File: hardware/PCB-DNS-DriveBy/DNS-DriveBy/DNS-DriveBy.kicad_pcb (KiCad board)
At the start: 2 copper layers, 76 x 40 mm, 21 parts, among them J1 JST 2.0, J2 Conn_01x04, J3 Conn_01x03, Q1 2N3904, Q2 2N3904, SW1 SW_SPST, U1 D1 Mini, U2 NEO-6M

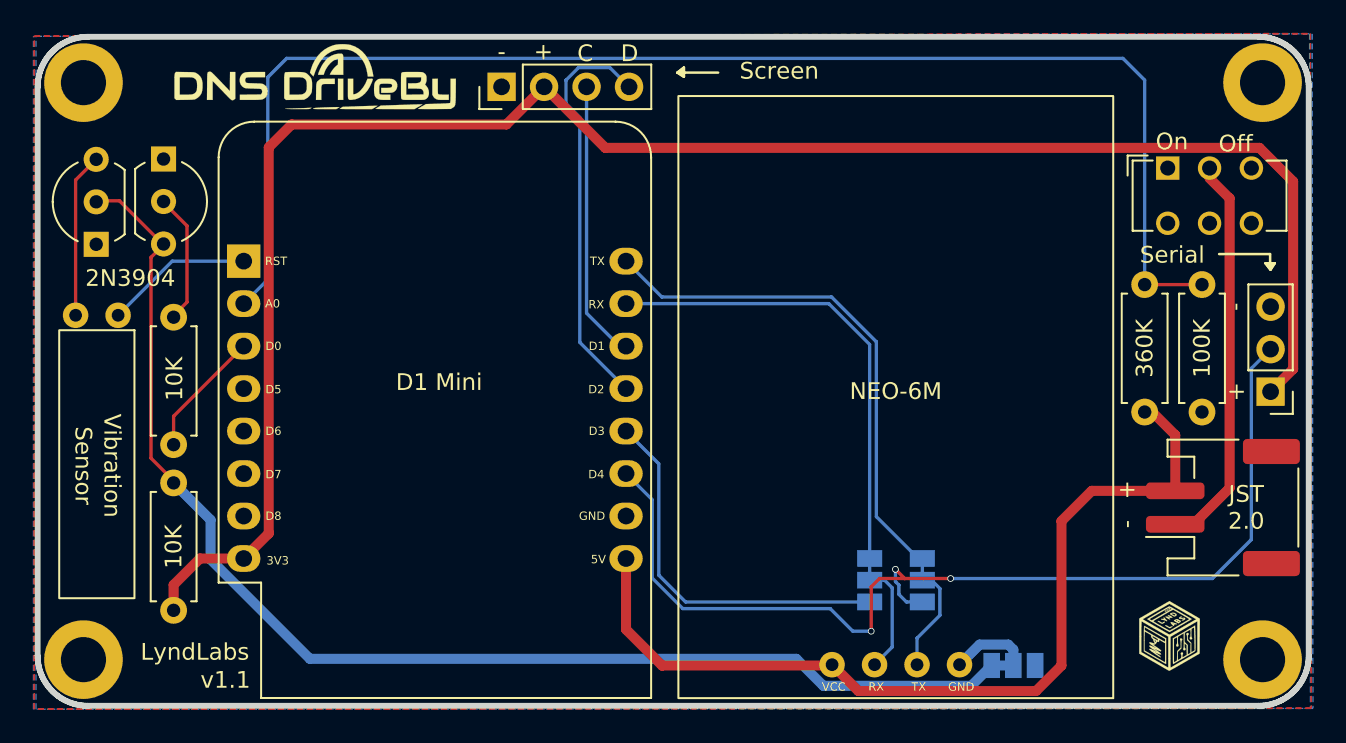
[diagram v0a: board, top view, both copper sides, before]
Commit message: fix low-power mode hardware, add jumper pads, graphics
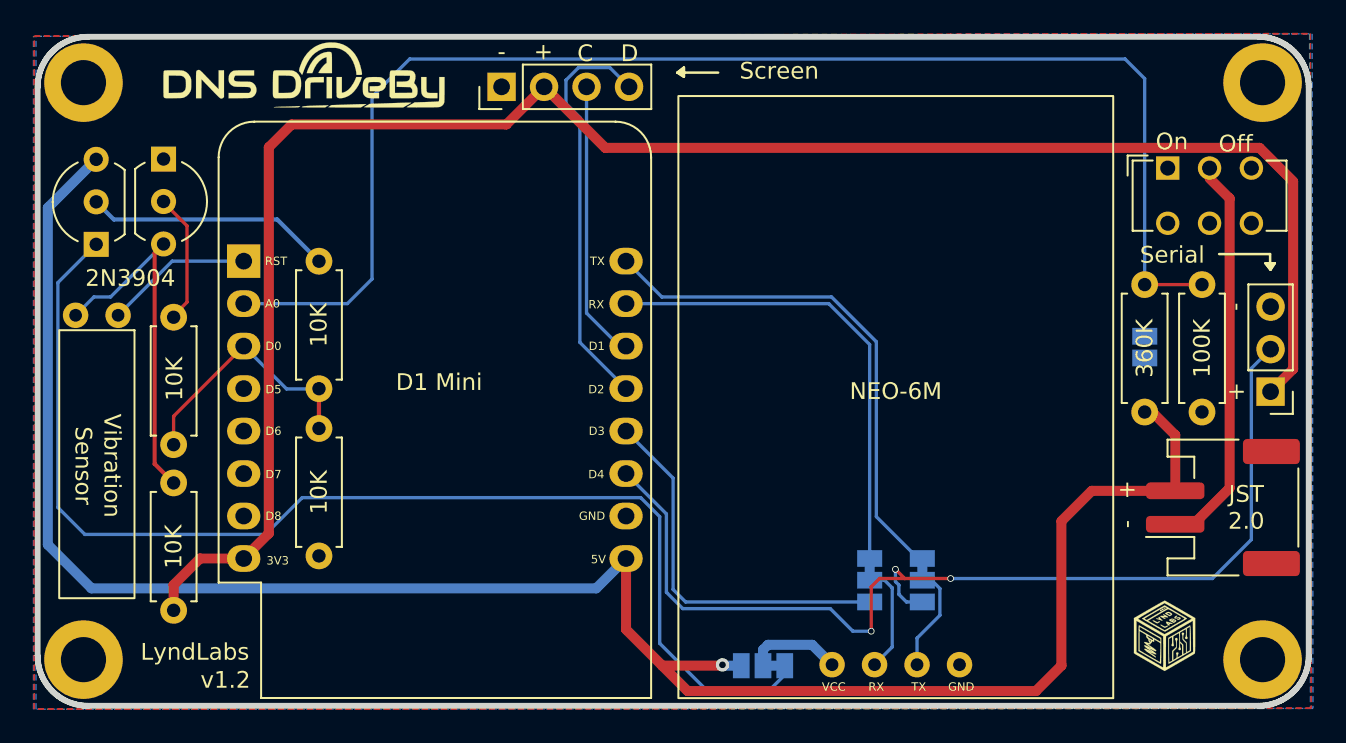
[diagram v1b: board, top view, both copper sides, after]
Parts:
- removed the Ref** at (26.4, 20.1)
- added JP4: Jumper_2_Open, Jumper:SolderJumper-2_P1.3mm_Open_Pad1.0x1.5mm, B.Cu at (67.0, 19.3)
- added R3: 10K, Resistor_THT:R_Axial_DIN0207_L6.3mm_D2.5mm_P7.62mm_Horizontal, F.Cu at (17.6, 31.8)
- added R4: 10K, Resistor_THT:R_Axial_DIN0207_L6.3mm_D2.5mm_P7.62mm_Horizontal, F.Cu at (17.6, 14.2)
- added Ref**: Val**, v1.0-pcb-art, F.Cu at (38.0, 20.5)
- JP1: renamed from GPS GND; value SolderJumper-3_P1.3mm_Open_Pad1.0x1.5mm -> GPS GND; footprint Jumper:SolderJumper-3_P1.3mm_Open_Pad1.0x1.5mm -> Jumper:SolderJumper-3_P1.3mm_Bridged12_Pad1.0x1.5mm
- JP2: renamed from RX; value SolderJumper-3_P1.3mm_Open_Pad1.0x1.5mm -> RX; footprint Jumper:SolderJumper-3_P1.3mm_Open_Pad1.0x1.5mm -> Jumper:SolderJumper-3_P1.3mm_Bridged12_Pad1.0x1.5mm
- JP3: renamed from TX; value SolderJumper-3_P1.3mm_Open_Pad1.0x1.5mm -> TX; footprint Jumper:SolderJumper-3_P1.3mm_Open_Pad1.0x1.5mm -> Jumper:SolderJumper-3_P1.3mm_Bridged12_Pad1.0x1.5mm
- moved JP1 15.0 mm to (44.1, 38.4)
- renumbered R3 to R5, R4 to R6
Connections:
- net TX1 renamed D4
- JP1 pad 1: GND -> Net-(JP1-Pad1)
- JP1 pad 2: GPS- -> Net-(JP1-Pad2)
- JP1 pad 3: GPS- -> +BATT
- JP2 pad 3: unconnected-(U1-Pad12) -> D3
- JP3 pad 2: GPS_TX -> Net-(JP3-Pad2)
- Q1 pad 3: GPS- -> Net-(Q1-Pad3)
- Q2 pad 1: GND -> Net-(JP1-Pad1)
- Q2 pad 2: GPS- -> Net-(Q2-Pad2)
- Q2 pad 3: Net-(Q2-Pad3) -> +BATT
- R2 pad 1: GPS- -> Net-(Q1-Pad3)
- U1 pad 12: unconnected-(U1-Pad12) -> D3
- U2 pad 1: +BATT -> Net-(JP1-Pad2)
- U2 pad 2: GPS_RX -> Net-(JP2-Pad2)
- U2 pad 3: GPS_TX -> Net-(JP3-Pad2)
- U2 pad 4: GPS- -> GND
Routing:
- net GPS-: track 82.0 -> 0.00 mm
- net Net-(JP1-Pad1): track 0.00 -> 71.8 mm
- net +BATT: track 54.6 -> 120.0 mm, vias 0 -> 1
- net unconnected-(U1-Pad12): track 22.7 -> 0.00 mm
- net D3: track 0.00 -> 22.7 mm
- net Net-(Q1-Pad3): track 0.00 -> 22.0 mm
- net Net-(Q2-Pad2): track 0.00 -> 14.8 mm
- net Net-(Q2-Pad3): track 9.83 -> 0.00 mm
- net D0: track 7.53 -> 15.5 mm
- net GPS_TX: track 38.9 -> 31.2 mm
- net GPS_RX: track 35.9 -> 28.4 mm
- net Net-(JP3-Pad2): track 0.00 -> 6.37 mm
- net Net-(JP2-Pad2): track 0.00 -> 6.27 mm
- net Net-(JP1-Pad2): track 0.00 -> 5.70 mm
- net A0: track 83.2 -> 82.5 mm
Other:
- board text added: "v1.2"
- board text removed: "dnsdriveby.com"
- board text removed: "v1.1"
